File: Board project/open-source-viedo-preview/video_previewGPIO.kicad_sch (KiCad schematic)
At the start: 8 parts, among them J1 7499110124

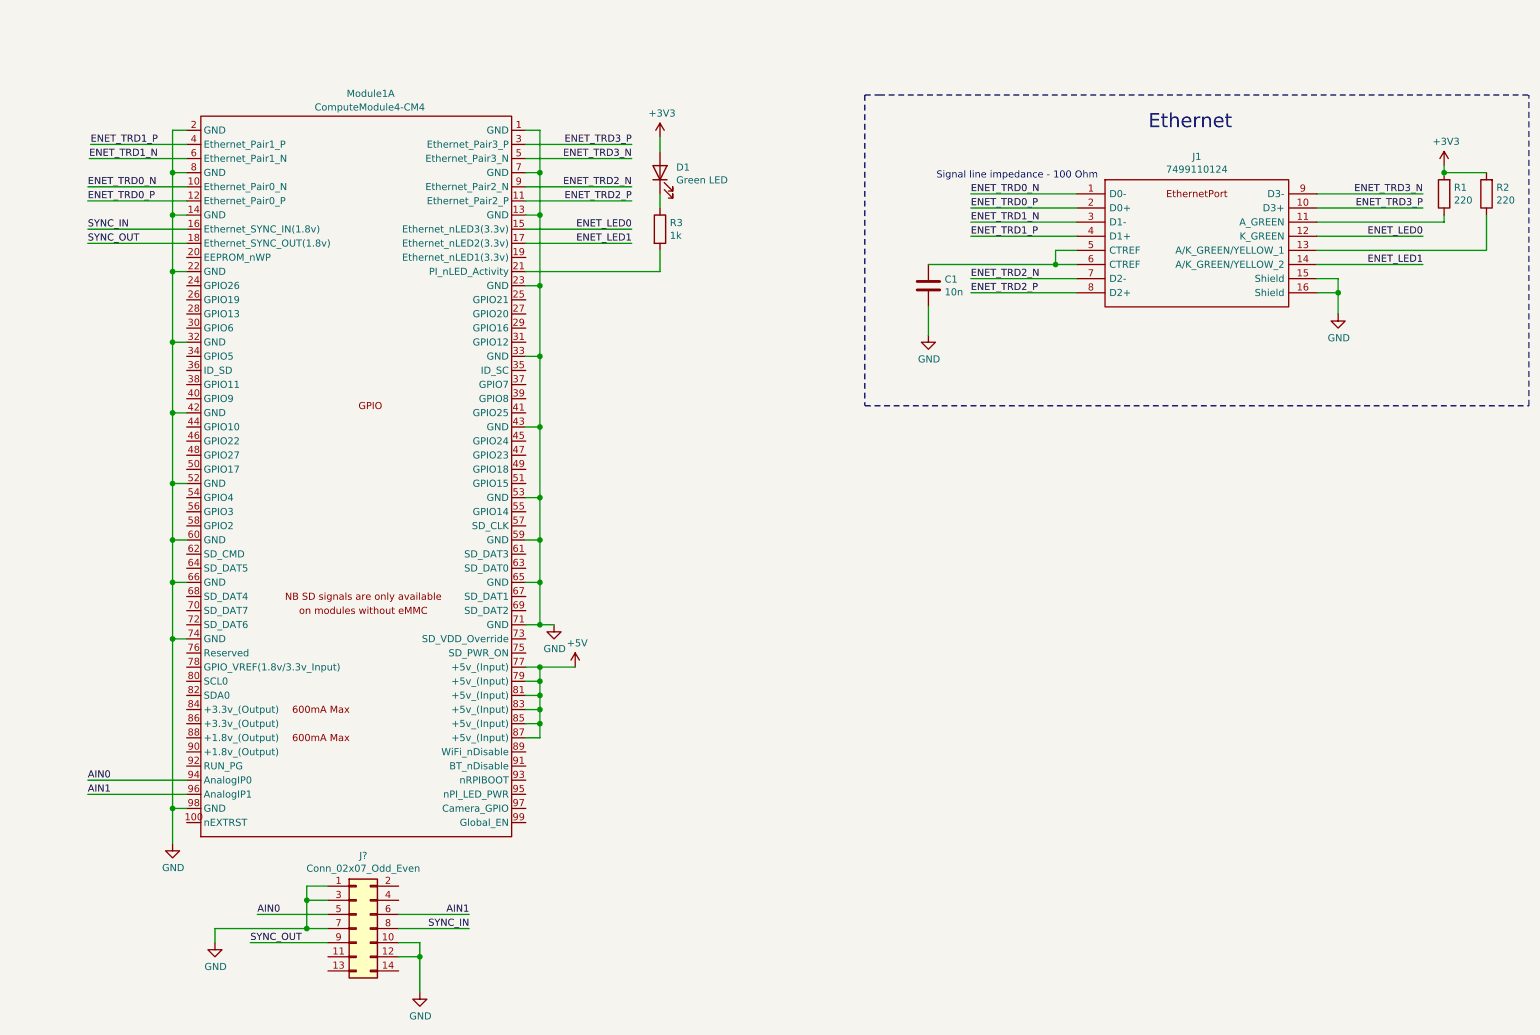
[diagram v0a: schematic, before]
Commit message: 40 GPIOs pins added
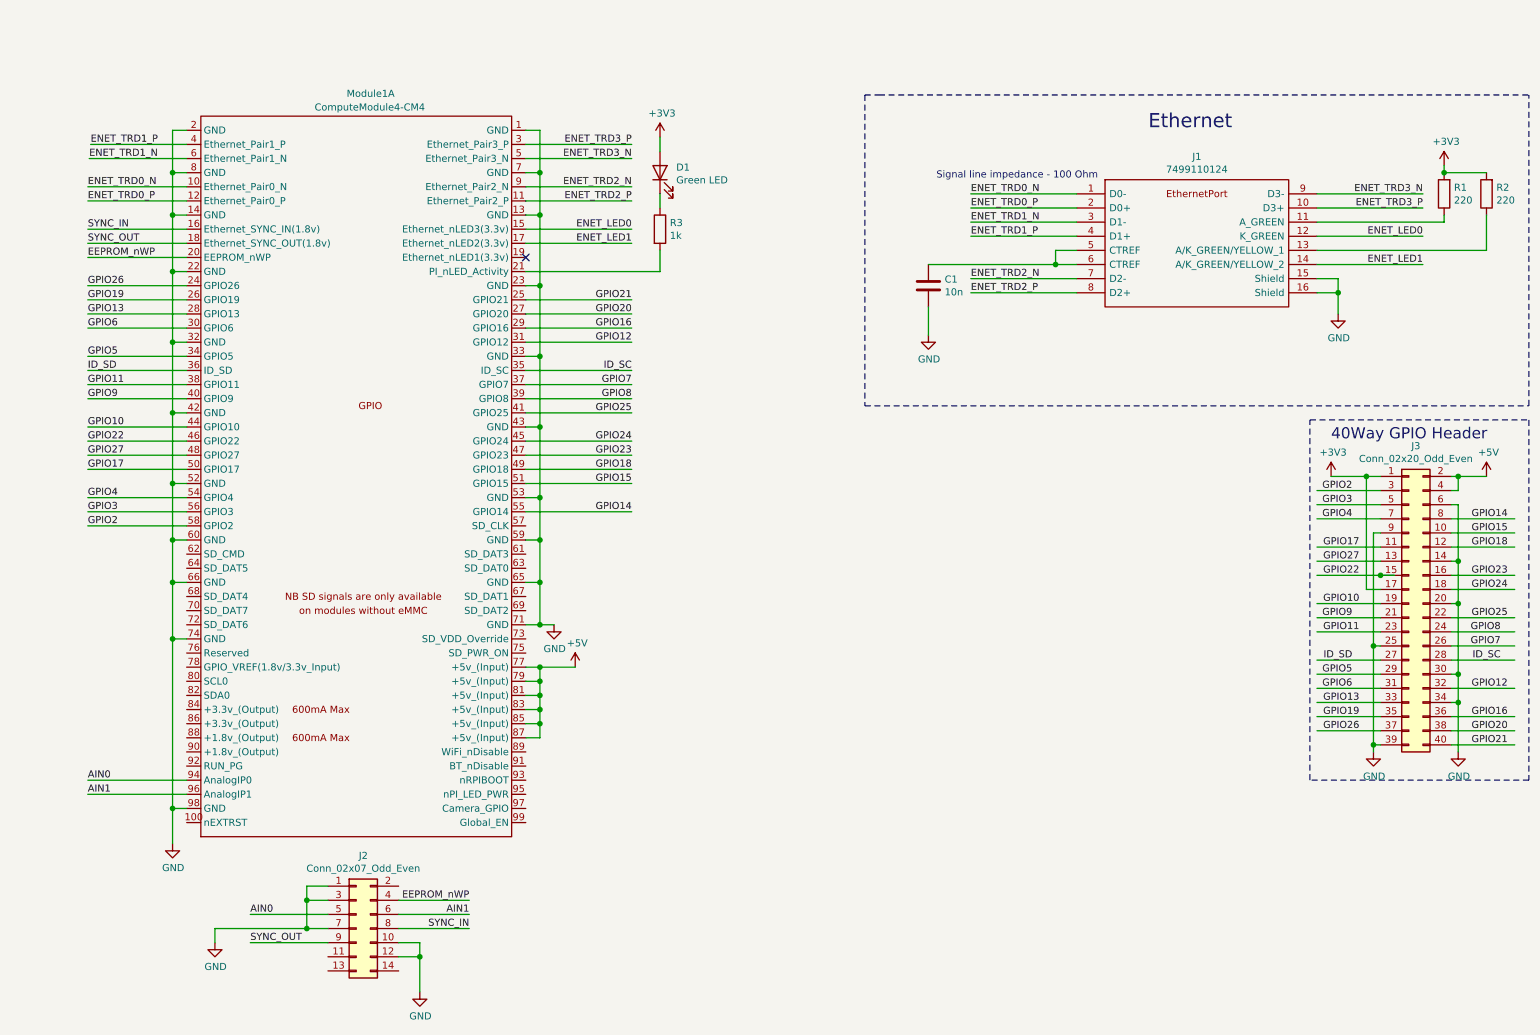
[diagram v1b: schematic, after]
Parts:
- added J3: Conn_02x20_Odd_Even, symbol Connector_Generic:Conn_02x20_Odd_Even
- gave numbers to parts that had none: 1
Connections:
- net +3V3: now also J3.1 (Pin_1), J3.17 (Pin_17)
- net +5V: now also J3.2 (Pin_2), J3.4 (Pin_4)
- net GND: now also J3.14 (Pin_14), J3.20 (Pin_20), J3.25 (Pin_25), J3.30 (Pin_30), J3.34 (Pin_34), J3.39 (Pin_39), J3.6 (Pin_6), J3.9 (Pin_9)
- net EEPROM_nWP: now reaches J2.4 (Pin_4)
- net EEPROM_nWP: now also Module1.20 (EEPROM_nWP)
- net GPIO26: now reaches Module1.24 (GPIO26)
- net GPIO26: now also J3.37 (Pin_37)
- net GPIO21: now reaches Module1.25 (GPIO21)
- net GPIO21: now also J3.40 (Pin_40)
- net GPIO19: now reaches Module1.26 (GPIO19)
- net GPIO19: now also J3.35 (Pin_35)
- net GPIO20: now reaches Module1.27 (GPIO20)
- net GPIO20: now also J3.38 (Pin_38)
- net GPIO13: now reaches Module1.28 (GPIO13)
- net GPIO13: now also J3.33 (Pin_33)
- net GPIO16: now reaches Module1.29 (GPIO16)
- net GPIO16: now also J3.36 (Pin_36)
- net GPIO6: now reaches Module1.30 (GPIO6)
- net GPIO6: now also J3.31 (Pin_31)
- net GPIO12: now reaches Module1.31 (GPIO12)
- net GPIO12: now also J3.32 (Pin_32)
- net GPIO5: now reaches Module1.34 (GPIO5)
- net GPIO5: now also J3.29 (Pin_29)
- net ID_SC: now reaches Module1.35 (ID_SC)
- net ID_SC: now also J3.28 (Pin_28)
- net ID_SD: now reaches Module1.36 (ID_SD)
- net ID_SD: now also J3.27 (Pin_27)
- net GPIO7: now reaches Module1.37 (GPIO7)
- net GPIO7: now also J3.26 (Pin_26)
- net GPIO11: now reaches Module1.38 (GPIO11)
- net GPIO11: now also J3.23 (Pin_23)
- net GPIO8: now reaches Module1.39 (GPIO8)
- net GPIO8: now also J3.24 (Pin_24)
- net GPIO9: now reaches Module1.40 (GPIO9)
- net GPIO9: now also J3.21 (Pin_21)
- net GPIO25: now reaches Module1.41 (GPIO25)
- net GPIO25: now also J3.22 (Pin_22)
- net GPIO10: now reaches Module1.44 (GPIO10)
- net GPIO10: now also J3.19 (Pin_19)
- net GPIO24: now reaches Module1.45 (GPIO24)
- net GPIO24: now also J3.18 (Pin_18)
- net GPIO22: now reaches Module1.46 (GPIO22)
- net GPIO22: now also J3.15 (Pin_15)
- net GPIO23: now reaches Module1.47 (GPIO23)
- net GPIO23: now also J3.16 (Pin_16)
- net GPIO27: now reaches Module1.48 (GPIO27)
- net GPIO27: now also J3.13 (Pin_13)
- net GPIO18: now reaches Module1.49 (GPIO18)
- net GPIO18: now also J3.12 (Pin_12)
- net GPIO17: now reaches Module1.50 (GPIO17)
- net GPIO17: now also J3.11 (Pin_11)
- net GPIO15: now reaches Module1.51 (GPIO15)
- net GPIO15: now also J3.10 (Pin_10)
- net GPIO4: now reaches Module1.54 (GPIO4)
- net GPIO4: now also J3.7 (Pin_7)
- net GPIO14: now reaches Module1.55 (GPIO14)
- net GPIO14: now also J3.8 (Pin_8)
- net GPIO3: now reaches Module1.56 (GPIO3)
- net GPIO3: now also J3.5 (Pin_5)
- net GPIO2: now reaches Module1.58 (GPIO2)
- net GPIO2: now also J3.3 (Pin_3)
- no-connect marks 0 -> 1
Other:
- note added: "40Way GPIO Header"

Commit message: Pins 51-100 and HighSpeed part with cam connector added.
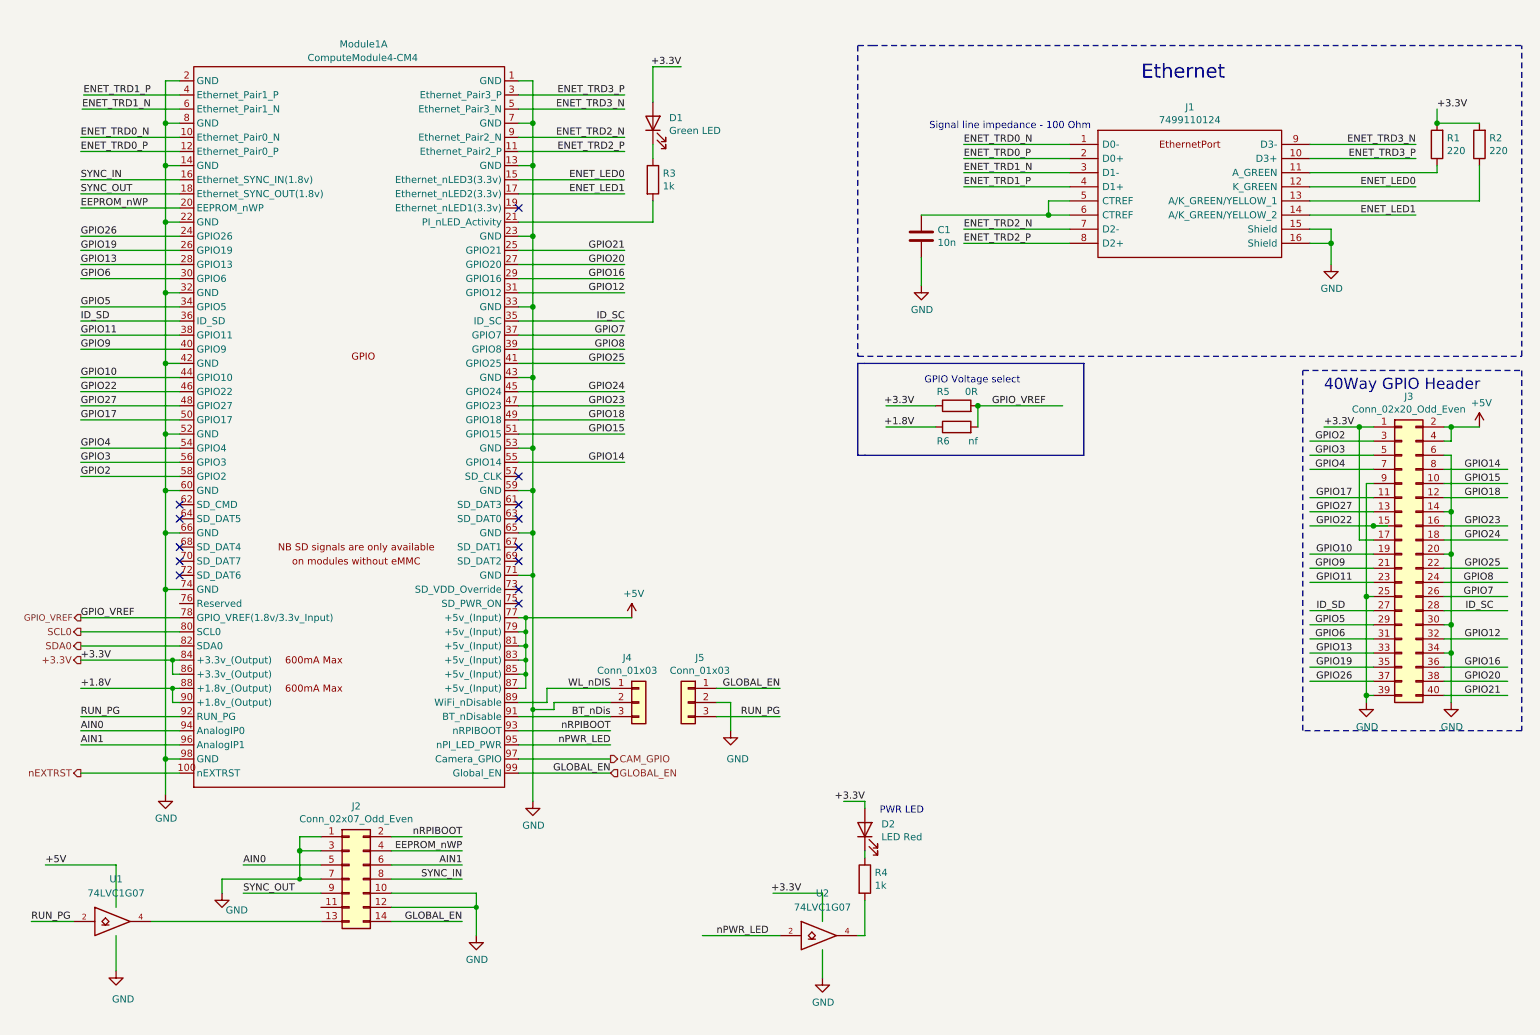
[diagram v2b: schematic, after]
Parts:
- added D2: LED Red, LED_SMD:LED_0603_1608Metric, symbol Device:LED
- added J4, J5: Conn_01x03, Connector_PinHeader_2.54mm:PinHeader_1x03_P2.54mm_Vertical, symbol Connector_Generic:Conn_01x03
- added R4: 1k, Resistor_SMD:R_0402_1005Metric, symbol Device:R
- added R5: 0R, Resistor_SMD:R_0805_2012Metric_Pad1.15x1.40mm_HandSolder, symbol Device:R
- added R6: nf, Resistor_SMD:R_0805_2012Metric_Pad1.15x1.40mm_HandSolder, symbol Device:R
- added U1, U2: 74LVC1G07, Package_TO_SOT_SMD:SOT-353_SC-70-5_Handsoldering, symbol 74xGxx:74LVC1G07
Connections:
- net +3V3 is gone; now on net +5V: D1.2 (A), J3.1 (Pin_1), J3.17 (Pin_17), R1.2, R2.2
- net +5V: now also Module1.84 (+3.3v_(Output)), Module1.86 (+3.3v_(Output)), D2.2 (A), R5.1, U1.5 (VCC), U2.5 (VCC)
- net GND: now also J4.2 (Pin_2), J5.2 (Pin_2), U1.3 (GND), U2.3 (GND)
- net at J2.13 (Pin_13): now also U1.4
- net GLOBAL_EN: now reaches J2.14 (Pin_14)
- net GLOBAL_EN: now also Module1.99 (Global_EN), J5.1 (Pin_1)
- net nRPIBOOT: now reaches J2.2 (Pin_2)
- net nRPIBOOT: now also Module1.93 (nRPIBOOT)
- net nEXTRST: now reaches Module1.100 (nEXTRST)
- net GPIO_VREF: now reaches Module1.78 (GPIO_VREF(1.8v/3.3v_Input))
- net GPIO_VREF: now also R5.2, R6.2
- net SCL0: now reaches Module1.80 (SCL0)
- net SDA0: now reaches Module1.82 (SDA0)
- net +1.8V: now reaches Module1.88 (+1.8v_(Output))
- net +1.8V: now also Module1.90 (+1.8v_(Output)), R6.1
- net WL_nDIS: now reaches Module1.89 (WiFi_nDisable)
- net WL_nDIS: now also J4.1 (Pin_1)
- net BT_nDis: now reaches Module1.91 (BT_nDisable)
- net BT_nDis: now also J4.3 (Pin_3)
- net RUN_PG: now reaches Module1.92 (RUN_PG)
- net RUN_PG: now also J5.3 (Pin_3), U1.2
- net nPWR_LED: now reaches Module1.95 (nPI_LED_PWR)
- net nPWR_LED: now also U2.2
- net CAM_GPIO: now reaches Module1.97 (Camera_GPIO)
- new net: R4.2, U2.4
- new net: D2.1 (K), R4.1
- no-connect marks 1 -> 13
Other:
- note added: "GPIO Voltage select"
- note added: "PWR LED"
- moved on the sheet: C1, D1, J1, J2, J3, Module1A, R1, R2, R3

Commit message: Imporoved electrical schematic
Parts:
- C1: footprint (none) -> Capacitor_SMD:C_1206_3216Metric_Pad1.33x1.80mm_HandSolder
- D1: footprint (none) -> LED_SMD:LED_1206_3216Metric_Pad1.42x1.75mm_HandSolder
- J11: renamed from J3; footprint (none) -> Connector_PinHeader_2.54mm:PinHeader_2x20_P2.54mm_Vertical
- J7: renamed from J2; footprint (none) -> Connector_PinHeader_2.54mm:PinHeader_2x07_P2.54mm_Vertical
- R1: renamed from R3; footprint (none) -> Resistor_SMD:R_1206_3216Metric_Pad1.30x1.75mm_HandSolder
- R3: renamed from R5; footprint Resistor_SMD:R_0805_2012Metric_Pad1.15x1.40mm_HandSolder -> Resistor_SMD:R_1206_3216Metric_Pad1.30x1.75mm_HandSolder
- R5: renamed from R1; footprint (none) -> Resistor_SMD:R_1206_3216Metric_Pad1.30x1.75mm_HandSolder
- R6: renamed from R2; footprint (none) -> Resistor_SMD:R_1206_3216Metric_Pad1.30x1.75mm_HandSolder
- renumbered J1 to J10, J4 to J8, J5 to J9, R4 to R2, R6 to R4
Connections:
- net +1.8V renamed +1V8
- net +5V renamed +3V3
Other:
- moved on the sheet: R4

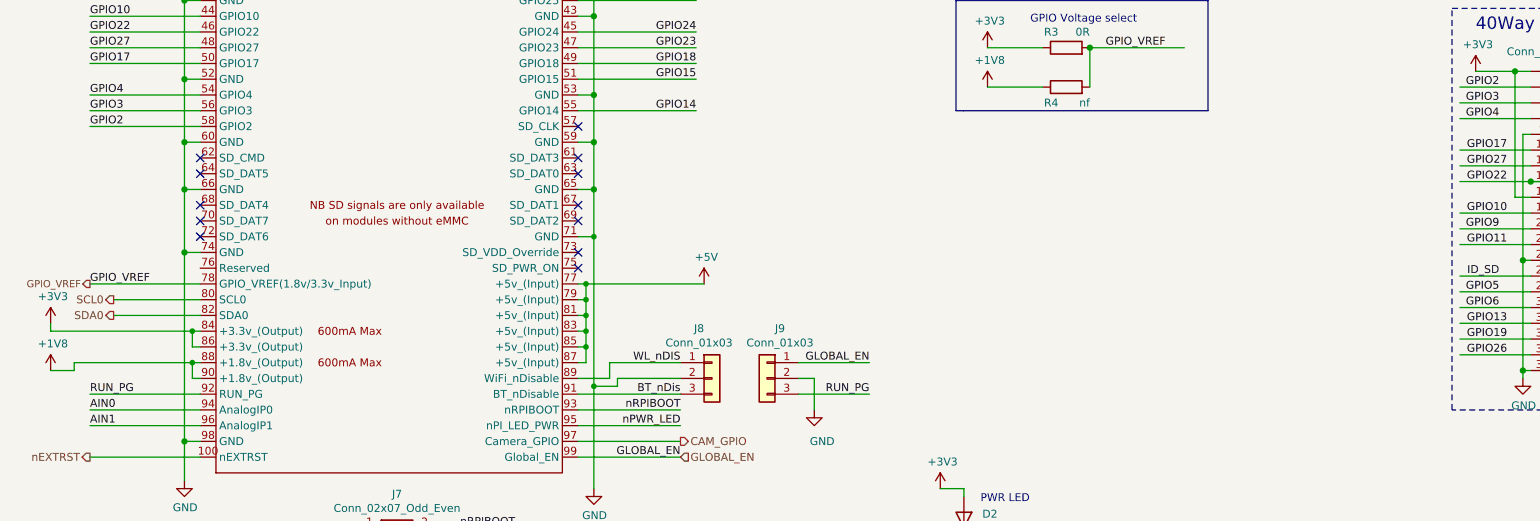
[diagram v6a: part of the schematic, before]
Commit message: Added SD Slot Card
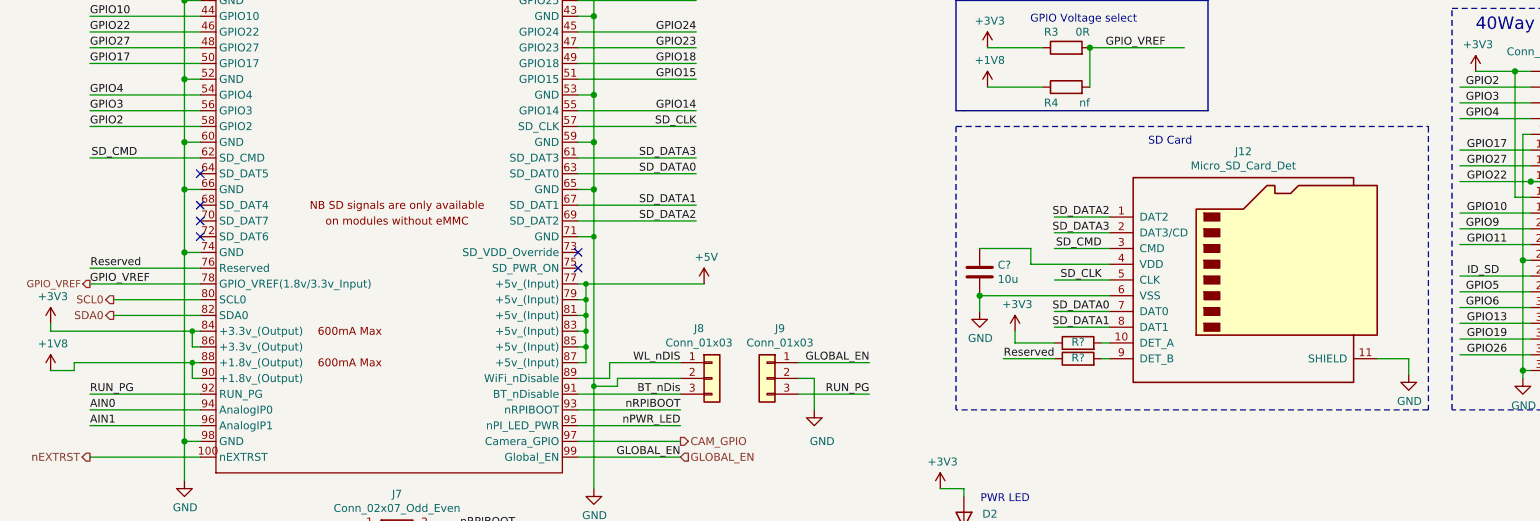
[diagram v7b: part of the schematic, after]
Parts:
- added C?: 10u, symbol Device:C
- added J12: Micro_SD_Card_Det, symbol Connector:Micro_SD_Card_Det
- added R? (x2): R, symbol Device:R
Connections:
- net +3V3: now also R?.1
- net GND: now also C?.2, J12.11 (SHIELD), J12.6 (VSS)
- net SD_CLK: now reaches Module1.57 (SD_CLK)
- net SD_CLK: now also J12.5 (CLK)
- net SD_DATA3: now reaches Module1.61 (SD_DAT3)
- net SD_DATA3: now also J12.2 (DAT3/CD)
- net SD_CMD: now reaches Module1.62 (SD_CMD)
- net SD_CMD: now also J12.3 (CMD)
- net SD_DATA0: now reaches Module1.63 (SD_DAT0)
- net SD_DATA0: now also J12.7 (DAT0)
- net SD_DATA1: now reaches Module1.67 (SD_DAT1)
- net SD_DATA1: now also J12.8 (DAT1)
- net SD_DATA2: now reaches Module1.69 (SD_DAT2)
- net SD_DATA2: now also J12.1 (DAT2)
- net Reserved: now reaches Module1.76 (Reserved)
- net Reserved: now also R?.1
- new net: C?.1, J12.4 (VDD)
- new net: J12.9 (DET_B), R?.2
- new net: J12.10 (DET_A), R?.2
- no-connect marks 13 -> 7
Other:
- note added: "SD Card"
